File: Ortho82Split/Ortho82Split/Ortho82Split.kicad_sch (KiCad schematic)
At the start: 119 parts, among them J1 Left-Right, J3 USB_C_Receptacle_USB2.0, J9 TC2030-IDC-NL, SW11 SW_Push, SW12 SW_Push, SW13 SW_Push, SW14 SW_Push, SW15 SW_Push, SW16 SW_Push, SW17 SW_Push, SW18 SW_Push, SW19 SW_Push, SW20 SW_Push, SW21 SW_Push, SW22 SW_Push, SW23 SW_Push, SW24 SW_Push, SW25 SW_Push, SW26 SW_Push, SW27 SW_Push, SW28 SW_Push, SW29 SW_Push, SW30 SW_Push, SW31 SW_Push, SW32 SW_Push, SW33 SW_Push, SW34 SW_Push, SW35 SW_Push, SW36 SW_Push, SW37 SW_Push, SW38 SW_Push, SW39 SW_Push, SW40 SW_Push, SW41 SW_Push, SW42 SW_Push, SW43 SW_Push, SW44 SW_Push, SW45 SW_Push, SW46 SW_Push, SW47 SW_Push, SW48 SW_Push, SW49 SW_Push, SW50 SW_Push, SW51 SW_Push, SW74 Left/Right, SW83 ~{RESET}, U1 MCP1700T-3302E_TT, U2 ATxmega32A4U-A, U3 USBLC6-2SC6

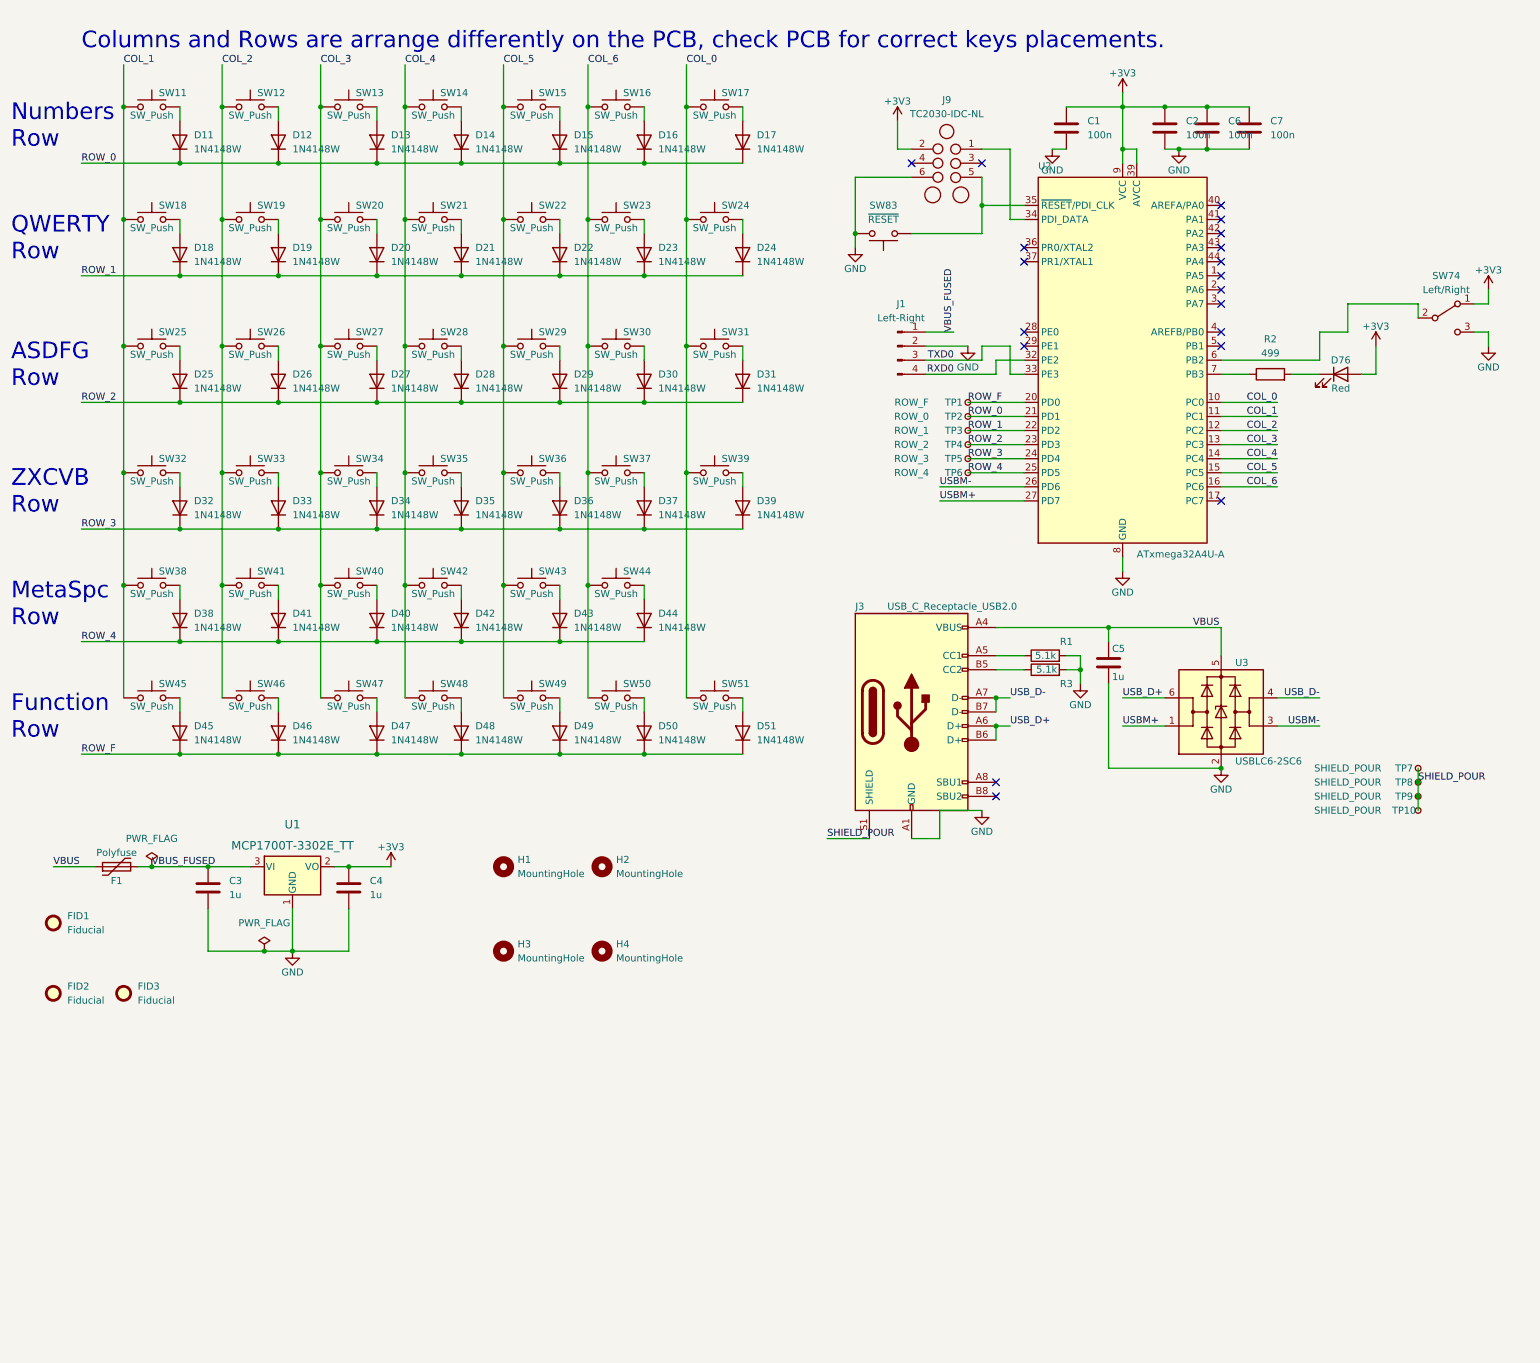
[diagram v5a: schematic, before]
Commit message: Correct spacing and kb2040 try.
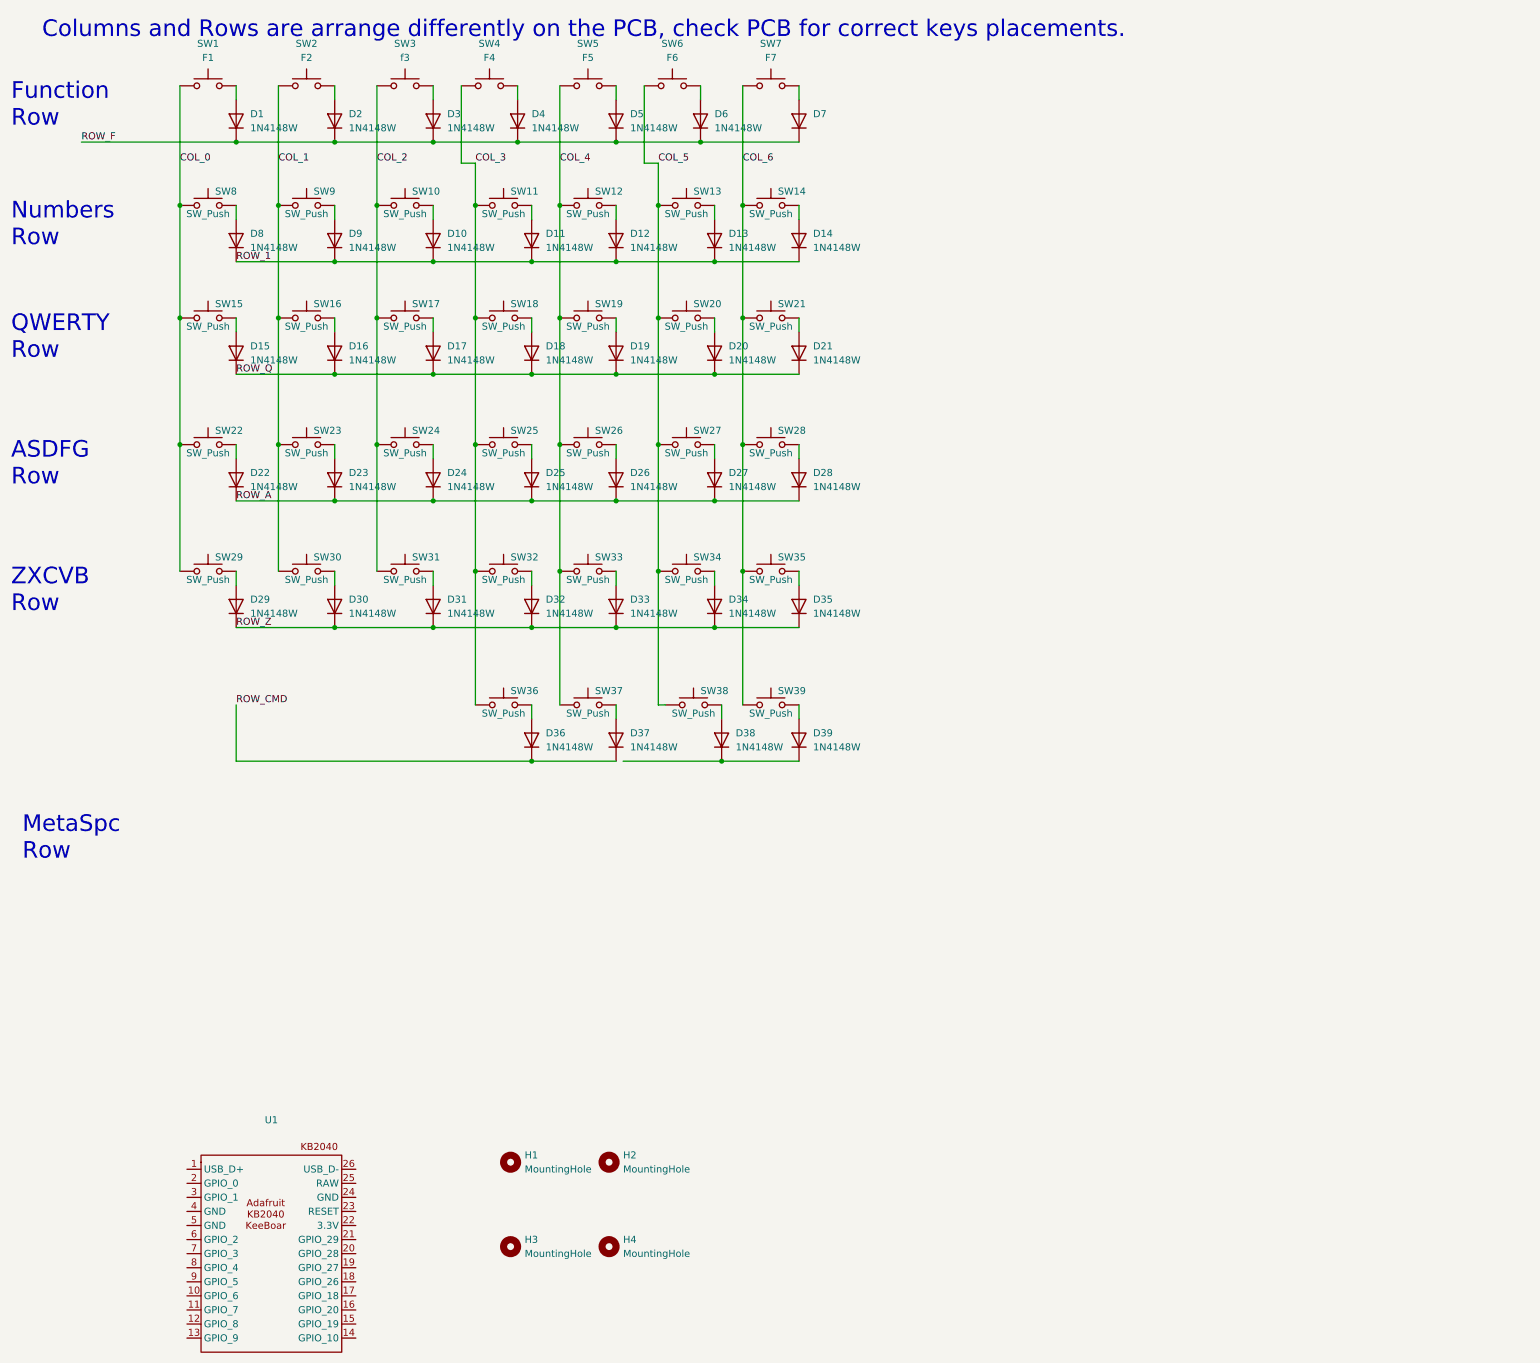
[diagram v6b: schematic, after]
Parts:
- removed C1, C2, C6, C7: 100n, Capacitor_SMD:C_0603_1608Metric_Pad1.08x0.95mm_HandSolder, symbol Device:C
- removed C3, C4, C5: 1u, Capacitor_SMD:C_0603_1608Metric_Pad1.08x0.95mm_HandSolder, symbol Device:C
- removed D38, D41: 1N4148W, HandsolderModifiedComponents:D_SOD-123F_DoubleSided, symbol Diode:1N4148W
- removed D76: Red, LED_THT:LED_D3.0mm, symbol Device:LED
- removed F1: Polyfuse, Fuse:Fuse_1206_3216Metric_Pad1.42x1.75mm_HandSolder, symbol Device:Polyfuse
- removed FID1, FID2, FID3: Fiducial, Fiducial:Fiducial_0.5mm_Mask1mm, symbol Mechanical:Fiducial
- removed J1: Left-Right, Connector_PinHeader_2.00mm:PinHeader_1x04_P2.00mm_Vertical, symbol Connector:Conn_01x04_Pin
- removed J3: USB_C_Receptacle_USB2.0, CustomHandSolderConnectors:USB_C_Receptacle_GCT_USB4085_HandSolder_SMT, symbol Connector:USB_C_Receptacle_USB2.0
- removed J9: TC2030-IDC-NL, Tag_Connect:TC2030-IDC-NL, symbol Tag-Connect:TC2030-IDC-NL
- removed R1, R3: 5.1k, Resistor_SMD:R_0805_2012Metric_Pad1.20x1.40mm_HandSolder, symbol Device:R
- removed R2: 499, Resistor_SMD:R_0805_2012Metric_Pad1.20x1.40mm_HandSolder, symbol Device:R
- removed SW38, SW41: SW_Push, Switch_Keyboard_Kailh:SW_Kailh_Choc_V1V2_1.00u, symbol Switch:SW_Push
- removed SW74: Left/Right, Jumper:SolderJumper-3_P1.3mm_Open_RoundedPad1.0x1.5mm_NumberLabels, symbol Switch:SW_SPDT
- removed SW83: ~{RESET}, Button_Switch_SMD:SW_Tactile_SPST_NO_Straight_CK_PTS636Sx25SMTRLFS, symbol Switch:SW_Push
- removed TP1: ROW_F, TestPoint:TestPoint_THTPad_1.5x1.5mm_Drill0.7mm, symbol Connector:TestPoint_Small
- removed TP10, TP7, TP8, TP9: SHIELD_POUR, TestPoint:TestPoint_THTPad_1.5x1.5mm_Drill0.7mm, symbol Connector:TestPoint_Small
- removed TP2: ROW_0, TestPoint:TestPoint_THTPad_1.5x1.5mm_Drill0.7mm, symbol Connector:TestPoint_Small
- removed TP3: ROW_1, TestPoint:TestPoint_THTPad_1.5x1.5mm_Drill0.7mm, symbol Connector:TestPoint_Small
- removed TP4: ROW_2, TestPoint:TestPoint_THTPad_1.5x1.5mm_Drill0.7mm, symbol Connector:TestPoint_Small
- removed TP5: ROW_3, TestPoint:TestPoint_THTPad_1.5x1.5mm_Drill0.7mm, symbol Connector:TestPoint_Small
- removed TP6: ROW_4, TestPoint:TestPoint_THTPad_1.5x1.5mm_Drill0.7mm, symbol Connector:TestPoint_Small
- removed U1: MCP1700T-3302E_TT, Package_TO_SOT_SMD:SOT-23, symbol Regulator_Linear:MCP1700x-330xxTT
- removed U2: ATxmega32A4U-A, Package_QFP:TQFP-44_10x10mm_P0.8mm, symbol MCU_Microchip_ATmega:ATxmega32A4U-A
- removed U3: USBLC6-2SC6, Package_TO_SOT_SMD:SOT-23-6, symbol Power_Protection:USBLC6-2SC6
- added U1: ~, Adafruit_KB2040:KB2040, symbol Adafruit DevBoards:KB2040
- D1: renamed from D45; footprint HandsolderModifiedComponents:D_SOD-123F_DoubleSided -> Diode_SMD:D_SOD-123
- D10: renamed from D12; footprint HandsolderModifiedComponents:D_SOD-123F_DoubleSided -> Diode_SMD:D_SOD-123
- D11: renamed from D13; footprint HandsolderModifiedComponents:D_SOD-123F_DoubleSided -> Diode_SMD:D_SOD-123
- D12: renamed from D14; footprint HandsolderModifiedComponents:D_SOD-123F_DoubleSided -> Diode_SMD:D_SOD-123
- D13: renamed from D15; footprint HandsolderModifiedComponents:D_SOD-123F_DoubleSided -> Diode_SMD:D_SOD-123
- D14: renamed from D16; footprint HandsolderModifiedComponents:D_SOD-123F_DoubleSided -> Diode_SMD:D_SOD-123
- D15: renamed from D24; footprint HandsolderModifiedComponents:D_SOD-123F_DoubleSided -> Diode_SMD:D_SOD-123
- D16: renamed from D18; footprint HandsolderModifiedComponents:D_SOD-123F_DoubleSided -> Diode_SMD:D_SOD-123
- D17: renamed from D19; footprint HandsolderModifiedComponents:D_SOD-123F_DoubleSided -> Diode_SMD:D_SOD-123
- D18: renamed from D20; footprint HandsolderModifiedComponents:D_SOD-123F_DoubleSided -> Diode_SMD:D_SOD-123
- D19: renamed from D21; footprint HandsolderModifiedComponents:D_SOD-123F_DoubleSided -> Diode_SMD:D_SOD-123
- D2: renamed from D46; footprint HandsolderModifiedComponents:D_SOD-123F_DoubleSided -> Diode_SMD:D_SOD-123
- D20: renamed from D22; footprint HandsolderModifiedComponents:D_SOD-123F_DoubleSided -> Diode_SMD:D_SOD-123
- D21: renamed from D23; footprint HandsolderModifiedComponents:D_SOD-123F_DoubleSided -> Diode_SMD:D_SOD-123
- D22: renamed from D31; footprint HandsolderModifiedComponents:D_SOD-123F_DoubleSided -> Diode_SMD:D_SOD-123
- D23: renamed from D25; footprint HandsolderModifiedComponents:D_SOD-123F_DoubleSided -> Diode_SMD:D_SOD-123
- D24: renamed from D26; footprint HandsolderModifiedComponents:D_SOD-123F_DoubleSided -> Diode_SMD:D_SOD-123
- D25: renamed from D27; footprint HandsolderModifiedComponents:D_SOD-123F_DoubleSided -> Diode_SMD:D_SOD-123
- D26: renamed from D28; footprint HandsolderModifiedComponents:D_SOD-123F_DoubleSided -> Diode_SMD:D_SOD-123
- D27: renamed from D29; footprint HandsolderModifiedComponents:D_SOD-123F_DoubleSided -> Diode_SMD:D_SOD-123
- D28: renamed from D30; footprint HandsolderModifiedComponents:D_SOD-123F_DoubleSided -> Diode_SMD:D_SOD-123
- D29: renamed from D39; footprint HandsolderModifiedComponents:D_SOD-123F_DoubleSided -> Diode_SMD:D_SOD-123
- D3: renamed from D47; footprint HandsolderModifiedComponents:D_SOD-123F_DoubleSided -> Diode_SMD:D_SOD-123
- D30: renamed from D32; footprint HandsolderModifiedComponents:D_SOD-123F_DoubleSided -> Diode_SMD:D_SOD-123
- D31: renamed from D33; footprint HandsolderModifiedComponents:D_SOD-123F_DoubleSided -> Diode_SMD:D_SOD-123
- D32: renamed from D34; footprint HandsolderModifiedComponents:D_SOD-123F_DoubleSided -> Diode_SMD:D_SOD-123
- D33: renamed from D35; footprint HandsolderModifiedComponents:D_SOD-123F_DoubleSided -> Diode_SMD:D_SOD-123
- D34: renamed from D36; footprint HandsolderModifiedComponents:D_SOD-123F_DoubleSided -> Diode_SMD:D_SOD-123
- D35: renamed from D37; footprint HandsolderModifiedComponents:D_SOD-123F_DoubleSided -> Diode_SMD:D_SOD-123
- D36: renamed from D40; footprint HandsolderModifiedComponents:D_SOD-123F_DoubleSided -> Diode_SMD:D_SOD-123
- D37: renamed from D42; footprint HandsolderModifiedComponents:D_SOD-123F_DoubleSided -> Diode_SMD:D_SOD-123
- D38: renamed from D43; footprint HandsolderModifiedComponents:D_SOD-123F_DoubleSided -> Diode_SMD:D_SOD-123
- D39: renamed from D44; footprint HandsolderModifiedComponents:D_SOD-123F_DoubleSided -> Diode_SMD:D_SOD-123
- D4: renamed from D48; footprint HandsolderModifiedComponents:D_SOD-123F_DoubleSided -> Diode_SMD:D_SOD-123
- D5: renamed from D49; footprint HandsolderModifiedComponents:D_SOD-123F_DoubleSided -> Diode_SMD:D_SOD-123
- D6: renamed from D50; footprint HandsolderModifiedComponents:D_SOD-123F_DoubleSided -> Diode_SMD:D_SOD-123
- D7: renamed from D51; footprint HandsolderModifiedComponents:D_SOD-123F_DoubleSided -> Diode_SMD:D_SOD-123
- D8: renamed from D17; footprint HandsolderModifiedComponents:D_SOD-123F_DoubleSided -> Diode_SMD:D_SOD-123
- D9: renamed from D11; footprint HandsolderModifiedComponents:D_SOD-123F_DoubleSided -> Diode_SMD:D_SOD-123
- SW1: renamed from SW45; value SW_Push -> F1; footprint Switch_Keyboard_Kailh:SW_Kailh_Choc_V1V2_1.00u -> Kailh Keyboard Switches:SW_Kailh_Choc_V1V2_1.00u
- SW10: renamed from SW12; footprint Switch_Keyboard_Kailh:SW_Kailh_Choc_V1V2_1.00u -> Kailh Keyboard Switches:SW_Kailh_Choc_V1V2_1.00u
- SW11: renamed from SW13; footprint Switch_Keyboard_Kailh:SW_Kailh_Choc_V1V2_1.00u -> Kailh Keyboard Switches:SW_Kailh_Choc_V1V2_1.00u
- SW12: renamed from SW14; footprint Switch_Keyboard_Kailh:SW_Kailh_Choc_V1V2_1.00u -> Kailh Keyboard Switches:SW_Kailh_Choc_V1V2_1.00u
- SW13: renamed from SW15; footprint Switch_Keyboard_Kailh:SW_Kailh_Choc_V1V2_1.00u -> Kailh Keyboard Switches:SW_Kailh_Choc_V1V2_1.00u
- SW14: renamed from SW16; footprint Switch_Keyboard_Kailh:SW_Kailh_Choc_V1V2_1.00u -> Kailh Keyboard Switches:SW_Kailh_Choc_V1V2_1.00u
- SW15: renamed from SW24; footprint Switch_Keyboard_Kailh:SW_Kailh_Choc_V1V2_1.50u -> Kailh Keyboard Switches:SW_Kailh_Choc_V1V2_1.50u
- SW16: renamed from SW18; footprint Switch_Keyboard_Kailh:SW_Kailh_Choc_V1V2_1.00u -> Kailh Keyboard Switches:SW_Kailh_Choc_V1V2_1.00u
- SW17: renamed from SW19; footprint Switch_Keyboard_Kailh:SW_Kailh_Choc_V1V2_1.00u -> Kailh Keyboard Switches:SW_Kailh_Choc_V1V2_1.00u
- SW18: renamed from SW20; footprint Switch_Keyboard_Kailh:SW_Kailh_Choc_V1V2_1.00u -> Kailh Keyboard Switches:SW_Kailh_Choc_V1V2_1.00u
- SW19: renamed from SW21; footprint Switch_Keyboard_Kailh:SW_Kailh_Choc_V1V2_1.00u -> Kailh Keyboard Switches:SW_Kailh_Choc_V1V2_1.00u
- SW2: renamed from SW46; value SW_Push -> F2; footprint Switch_Keyboard_Kailh:SW_Kailh_Choc_V1V2_1.00u -> Kailh Keyboard Switches:SW_Kailh_Choc_V1V2_1.00u
- SW20: renamed from SW22; footprint Switch_Keyboard_Kailh:SW_Kailh_Choc_V1V2_1.00u -> Kailh Keyboard Switches:SW_Kailh_Choc_V1V2_1.00u
- SW21: renamed from SW23; footprint Switch_Keyboard_Kailh:SW_Kailh_Choc_V1V2_1.00u -> Kailh Keyboard Switches:SW_Kailh_Choc_V1V2_1.00u
- SW22: renamed from SW31; footprint Switch_Keyboard_Kailh:SW_Kailh_Choc_V1V2_1.50u -> Kailh Keyboard Switches:SW_Kailh_Choc_V1V2_1.50u
- SW23: renamed from SW25; footprint Switch_Keyboard_Kailh:SW_Kailh_Choc_V1V2_1.00u -> Kailh Keyboard Switches:SW_Kailh_Choc_V1V2_1.00u
- SW24: renamed from SW26; footprint Switch_Keyboard_Kailh:SW_Kailh_Choc_V1V2_1.00u -> Kailh Keyboard Switches:SW_Kailh_Choc_V1V2_1.00u
- SW25: renamed from SW27; footprint Switch_Keyboard_Kailh:SW_Kailh_Choc_V1V2_1.00u -> Kailh Keyboard Switches:SW_Kailh_Choc_V1V2_1.00u
- SW26: renamed from SW28; footprint Switch_Keyboard_Kailh:SW_Kailh_Choc_V1V2_1.00u -> Kailh Keyboard Switches:SW_Kailh_Choc_V1V2_1.00u
- SW27: renamed from SW29; footprint Switch_Keyboard_Kailh:SW_Kailh_Choc_V1V2_1.00u -> Kailh Keyboard Switches:SW_Kailh_Choc_V1V2_1.00u
- SW28: renamed from SW30; footprint Switch_Keyboard_Kailh:SW_Kailh_Choc_V1V2_1.00u -> Kailh Keyboard Switches:SW_Kailh_Choc_V1V2_1.00u
- SW29: renamed from SW39; footprint Switch_Keyboard_Kailh:SW_Kailh_Choc_V1V2_1.50u -> Kailh Keyboard Switches:SW_Kailh_Choc_V1V2_1.50u
- SW3: renamed from SW47; value SW_Push -> f3; footprint Switch_Keyboard_Kailh:SW_Kailh_Choc_V1V2_1.00u -> Kailh Keyboard Switches:SW_Kailh_Choc_V1V2_1.00u
- SW30: renamed from SW32; footprint Switch_Keyboard_Kailh:SW_Kailh_Choc_V1V2_1.00u -> Kailh Keyboard Switches:SW_Kailh_Choc_V1V2_1.00u
- SW31: renamed from SW33; footprint Switch_Keyboard_Kailh:SW_Kailh_Choc_V1V2_1.00u -> Kailh Keyboard Switches:SW_Kailh_Choc_V1V2_1.00u
- SW32: renamed from SW34; footprint Switch_Keyboard_Kailh:SW_Kailh_Choc_V1V2_1.00u -> Kailh Keyboard Switches:SW_Kailh_Choc_V1V2_1.00u
- SW33: renamed from SW35; footprint Switch_Keyboard_Kailh:SW_Kailh_Choc_V1V2_1.00u -> Kailh Keyboard Switches:SW_Kailh_Choc_V1V2_1.00u
- SW34: renamed from SW36; footprint Switch_Keyboard_Kailh:SW_Kailh_Choc_V1V2_1.00u -> Kailh Keyboard Switches:SW_Kailh_Choc_V1V2_1.00u
- SW35: renamed from SW37; footprint Switch_Keyboard_Kailh:SW_Kailh_Choc_V1V2_1.00u -> Kailh Keyboard Switches:SW_Kailh_Choc_V1V2_1.00u
- SW36: renamed from SW40; footprint Switch_Keyboard_Kailh:SW_Kailh_Choc_V1V2_1.00u -> Kailh Keyboard Switches:SW_Kailh_Choc_V1V2_1.00u
- SW37: renamed from SW42; footprint Switch_Keyboard_Kailh:SW_Kailh_Choc_V1V2_1.00u -> Kailh Keyboard Switches:SW_Kailh_Choc_V1V2_1.00u
- SW38: renamed from SW43; footprint Switch_Keyboard_Kailh:SW_Kailh_Choc_V1V2_1.00u -> Kailh Keyboard Switches:SW_Kailh_Choc_V1V2_1.00u
- SW39: renamed from SW44; footprint Switch_Keyboard_Kailh:SW_Kailh_Choc_V1V2_1.50u -> Kailh Keyboard Switches:SW_Kailh_Choc_V1V2_1.00u
- SW4: renamed from SW48; value SW_Push -> F4; footprint Switch_Keyboard_Kailh:SW_Kailh_Choc_V1V2_1.00u -> Kailh Keyboard Switches:SW_Kailh_Choc_V1V2_1.00u
- SW5: renamed from SW49; value SW_Push -> F5; footprint Switch_Keyboard_Kailh:SW_Kailh_Choc_V1V2_1.00u -> Kailh Keyboard Switches:SW_Kailh_Choc_V1V2_1.00u
- SW6: renamed from SW50; value SW_Push -> F6; footprint Switch_Keyboard_Kailh:SW_Kailh_Choc_V1V2_1.00u -> Kailh Keyboard Switches:SW_Kailh_Choc_V1V2_1.00u
- SW7: renamed from SW51; value SW_Push -> F7; footprint Switch_Keyboard_Kailh:SW_Kailh_Choc_V1V2_1.50u -> Kailh Keyboard Switches:SW_Kailh_Choc_V1V2_1.50u
- SW8: renamed from SW17; footprint Switch_Keyboard_Kailh:SW_Kailh_Choc_V1V2_1.50u -> Kailh Keyboard Switches:SW_Kailh_Choc_V1V2_1.50u
- SW9: renamed from SW11; footprint Switch_Keyboard_Kailh:SW_Kailh_Choc_V1V2_1.00u -> Kailh Keyboard Switches:SW_Kailh_Choc_V1V2_1.00u
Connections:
- net ROW_0 is gone; now on net ROW_1: D10.1 (K), D11.1 (K), D12.1 (K), D13.1 (K), D14.1 (K), D8.1 (K), D9.1 (K)
- net COL_0: now also SW1.1; no longer SW7.1
- net COL_1: now also SW2.1; no longer SW1.1
- net COL_2: now also SW3.1; no longer SW2.1
- net COL_3: now also SW4.1; no longer SW3.1
- net COL_4: now also SW5.1; no longer SW4.1
- net COL_5: now also SW6.1; no longer SW5.1
- net COL_6: now also SW7.1; no longer SW6.1
- net ROW_1: no longer D15.1 (K), D16.1 (K), D17.1 (K), D18.1 (K), D19.1 (K), D20.1 (K), D21.1 (K)
- net ROW_2 renamed ROW_A
- net ROW_3 renamed ROW_Z
- net ROW_4: no longer names the net of D38.1 (K), D39.1 (K)
- net ROW_4: no longer D36.1 (K), D37.1 (K)
- new net ROW_CMD: D36.1 (K), D37.1 (K)
- new net ROW_Q: D15.1 (K), D16.1 (K), D17.1 (K), D18.1 (K), D19.1 (K), D20.1 (K), D21.1 (K)
- no-connect marks 19 -> 0
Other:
- moved on the sheet: D1, D10, D11, D12, D13, D14, D15, D16, D17, D18, D19, D2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
